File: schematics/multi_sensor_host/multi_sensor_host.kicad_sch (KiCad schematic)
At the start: 54 parts, among them J1 esp_rst, J10 swd, J11 stm_boot, J12 DC37_Receptacle_MountingHoles, J2 esp_flash_wifi, J3 esp_boot, J4 esp_flash_port, J5 tx, J6 MY_USB_B, J7 rst, J8 rx, J9 uart1, U8 MCP73812T-420I-OT, Y1 Crystal

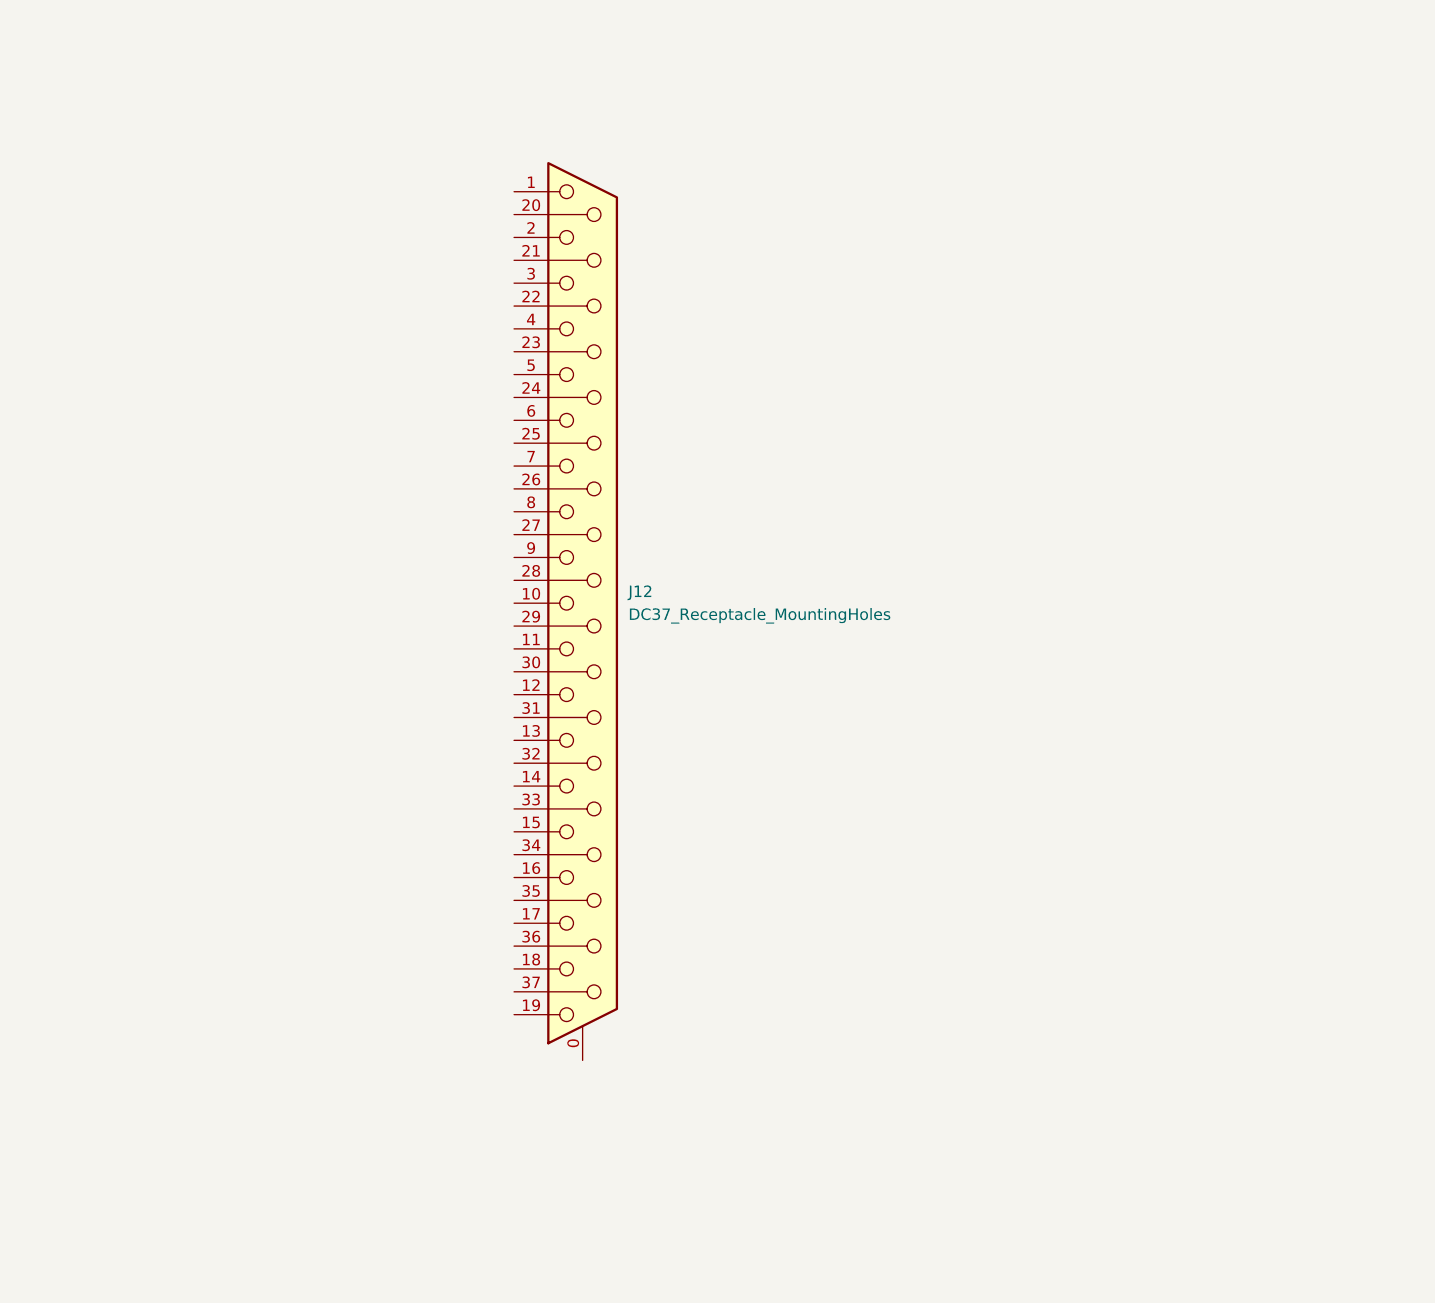
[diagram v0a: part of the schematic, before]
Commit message: Added two 27 pin sockets.
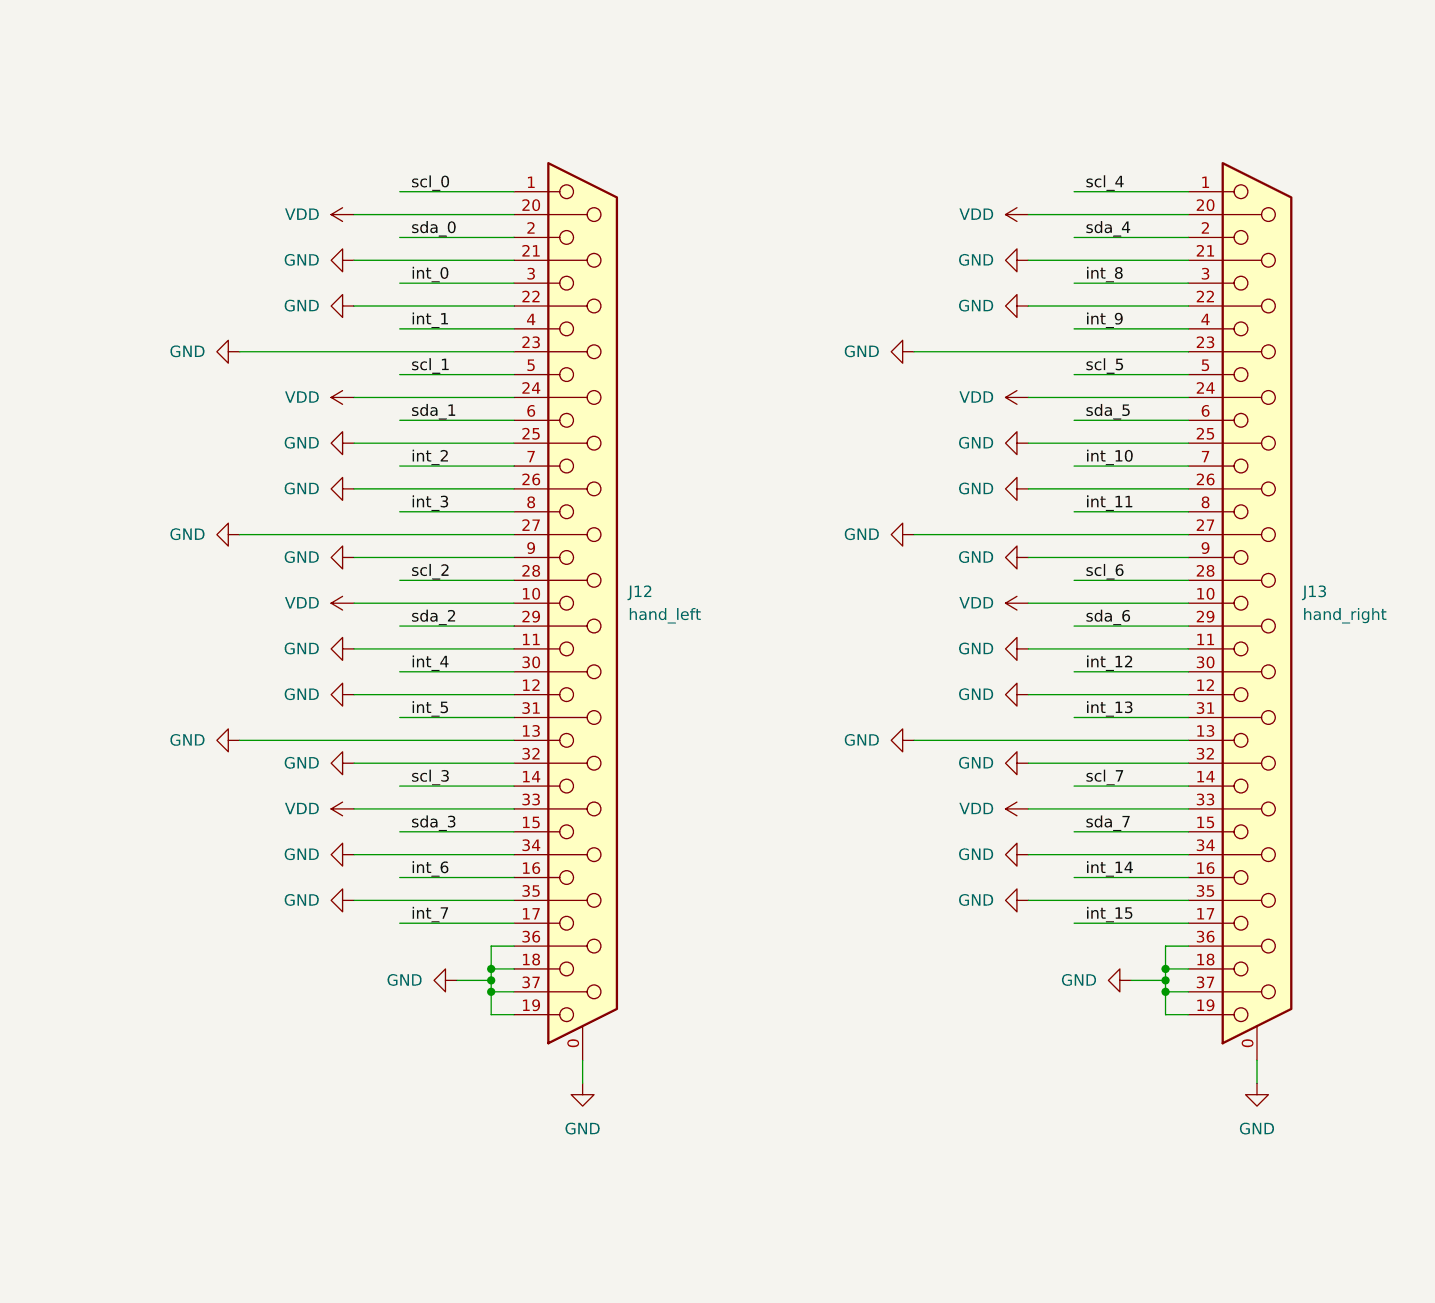
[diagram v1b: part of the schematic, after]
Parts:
- added J13: hand_right, symbol Connector:DC37_Receptacle_MountingHoles
- J12: value DC37_Receptacle_MountingHoles -> hand_left
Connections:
- net GND: now also J12.0 (PAD), J12.11, J12.12, J12.13, J12.18, J12.19, J12.21, J12.22, J12.23, J12.25, J12.26, J12.27, J12.32, J12.34, J12.35, J12.36, J12.37, J12.9, J13.0 (PAD), J13.11, J13.12, J13.13, J13.18, J13.19, J13.21, J13.22, J13.23, J13.25, J13.26, J13.27, J13.32, J13.34, J13.35, J13.36, J13.37, J13.9
- net VDD: now also J12.10, J12.20, J12.24, J12.33, J13.10, J13.20, J13.24, J13.33
- net int_0: now also J12.3
- net int_1: now also J12.4
- net int_10: now also J13.7
- net int_11: now also J13.8
- net int_12: now also J13.30
- net int_13: now also J13.31
- net int_14: now also J13.16
- net int_15: now also J13.17
- net int_2: now also J12.7
- net int_3: now also J12.8
- net int_5: now also J12.31
- net int_6: now also J12.16
- net int_7: now also J12.17
- net int_8: now also J13.3
- net int_9: now also J13.4
- net scl_0: now also J12.1
- net scl_1: now also J12.5
- net scl_2: now also J12.28
- net scl_3: now also J12.14
- net scl_4: now also J13.1
- net scl_5: now also J13.5
- net scl_6: now also J13.28
- net scl_7: now also J13.14
- net sda_0: now also J12.2
- net sda_1: now also J12.6
- net sda_2: now also J12.29
- net sda_3: now also J12.15
- net sda_4: now also J13.2
- net sda_5: now also J13.6
- net sda_6: now also J13.29
- net sda_7: now also J13.15
- net int_4: now reaches J12.30

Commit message: Added all 5 sockets.
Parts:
- added J14: leg_left, symbol Connector:DC37_Receptacle_MountingHoles
- added J15: leg_right, symbol Connector:DC37_Receptacle_MountingHoles
- added J16: torso_head, symbol Connector:DC37_Receptacle_MountingHoles
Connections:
- net GND: now also J14.0 (PAD), J14.18, J14.19, J14.21, J14.22, J14.23, J14.25, J14.26, J14.27, J14.36, J14.37, J15.0 (PAD), J15.18, J15.19, J15.21, J15.22, J15.23, J15.25, J15.26, J15.27, J15.36, J15.37, J16.0 (PAD), J16.11, J16.12, J16.13, J16.17, J16.18, J16.19, J16.21, J16.22, J16.23, J16.25, J16.26, J16.27, J16.32, J16.34, J16.35, J16.36, J16.37, J16.9; no longer J13.36
- net VDD: now also J14.20, J14.24, J15.20, J15.24, J16.10, J16.20, J16.24, J16.33
- net int_10: now also J13.8; no longer J13.7
- net int_11: now also J13.30; no longer J13.8
- net int_12: now also J13.31; no longer J13.30
- net int_13: now also J13.16; no longer J13.31
- net int_14: now also J14.3; no longer J13.16
- net int_15: now also J14.4; no longer J13.17
- net int_16: now also J14.7
- net int_17: now also J14.8
- net int_18: now also J15.3
- net int_19: now also J15.4
- net int_20: now also J15.7
- net int_21: now also J15.8
- net int_22: now also J16.3
- net int_23: now also J16.4
- net int_24: now also J16.7
- net int_25: now also J16.8
- net int_26: now also J16.30
- net int_27: now also J16.31
- net int_28: now also J16.16
- net int_29: now also J12.17
- net int_30: now also J13.17
- net int_31: now also J13.36
- net int_7: now also J13.3; no longer J12.17
- net int_8: now also J13.4; no longer J13.3
- net int_9: now also J13.7; no longer J13.4
- net scl_10: now also J15.1
- net scl_11: now also J15.5
- net scl_12: now also J16.1
- net scl_13: now also J16.5
- net scl_14: now also J16.28
- net scl_15: now also J16.14
- net scl_8: now also J14.1
- net scl_9: now also J14.5
- net sda_10: now also J15.2
- net sda_11: now also J15.6
- net sda_12: now also J16.2
- net sda_13: now also J16.6
- net sda_14: now also J16.29
- net sda_15: now also J16.15
- net sda_8: now also J14.2
- net sda_9: now also J14.6
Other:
- moved on the sheet: J12, J13

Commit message: No errors, no warnings.
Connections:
- net eps_tx is gone; now on net esp_tx: J4.3 (Pin_3), U7.16 (IO_1/UART0_TX)
- net GND: now also J14.10, J14.11, J14.12, J14.13, J14.14, J14.15, J14.16, J14.17, J14.28, J14.29, J14.30, J14.31, J14.32, J14.33, J14.34, J14.35, J14.9, J15.10, J15.11, J15.12, J15.13, J15.14, J15.15, J15.16, J15.17, J15.28, J15.29, J15.30, J15.31, J15.32, J15.33, J15.34, J15.35, J15.9

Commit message: Replaced ESP-21S with BM71 Microchip UART BLE module.
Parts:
- removed J1: esp_rst, symbol Connector:Conn_01x02_Pin
- removed J12: hand_left, symbol Connector:DC37_Receptacle_MountingHoles
- removed J13: hand_right, symbol Connector:DC37_Receptacle_MountingHoles
- removed J14: leg_left, symbol Connector:DC37_Receptacle_MountingHoles
- removed J15: leg_right, symbol Connector:DC37_Receptacle_MountingHoles
- removed J16: torso_head, symbol Connector:DC37_Receptacle_MountingHoles
- removed J2: esp_flash_wifi, symbol Connector:Conn_01x02_Pin
- removed J4: esp_flash_port, symbol Connector:Conn_01x04_Pin
- removed U7: ~, esp-12s:ESP-12S, symbol esp_12s:ESP-12S
- added C22, C32, C33, C34, C35: 4u7, Capacitors_SMD:C_0603, symbol Device:C
- added D5: LED, LED_THT:LED_D3.0mm, symbol Device:LED
- added J1, J18, J19, J2, J20, J21, J22, J23, J24, J25, J26, J27, J28, J29, J30, J4: RJ45, symbol Connector:RJ45
- added J17: bm_rst, symbol Connector:Conn_01x02_Pin
- added R96, R97: 10k, Resistors_SMD:R_0603, symbol Device:R
- added R98: 1k 5%, Resistor_SMD:R_0603_1608Metric, symbol Device:R
- added TP3: bm_cfg, symbol Connector:TestPoint
- added TP4: bm_vdd, symbol Connector:TestPoint
- added TP5: bm_tx, symbol Connector:TestPoint
- added TP6: bm_rx, symbol Connector:TestPoint
- added TP7: bm_gnd, symbol Connector:TestPoint
- added TP8: bm_rst, symbol Connector:TestPoint
- added U7: BM71BLES1FC2-0B02AA, BM71BLES1FC2_MCH, symbol BM71BLES1FC2:BM71BLES1FC2-0B02AA
- J3: value esp_boot -> bm_cfg
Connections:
- net GND: now also C22.2, C32.2, C33.2, C34.2, C35.2, J1.2, J1.4, J17.2 (Pin_2), J18.2, J18.4, J19.2, J19.4, J2.2, J2.4, J20.2, J20.4, J21.2, J21.4, J22.2, J22.4, J23.2, J23.4, J24.2, J24.4, J25.2, J25.4, J26.2, J26.4, J27.2, J27.4, J28.2, J28.4, J29.2, J29.4, J30.2, J30.4, J4.2, J4.4, TP7.1, U7.13 (GND), U7.2 (GND)
- net VDD: now also C33.1, C34.1, C35.1, J1.6, J1.8, J18.6, J18.8, J19.6, J19.8, J2.6, J2.8, J20.6, J20.8, J21.6, J21.8, J22.6, J22.8, J23.6, J23.8, J24.6, J24.8, J25.6, J25.8, J26.6, J26.8, J27.6, J27.8, J28.6, J28.8, J29.6, J29.8, J30.6, J30.8, J4.6, J4.8, R96.1, R97.1, R98.1, TP4.1, U7.14 (VBAT)
- net int_0: now also J1.5
- net int_1: now also J1.7
- net int_10: now also J20.7
- net int_11: now also J21.5
- net int_12: now also J21.7
- net int_13: now also J22.5
- net int_14: now also J23.5
- net int_15: now also J23.7
- net int_16: now also J24.5
- net int_17: now also J24.7
- net int_18: now also J25.5
- net int_19: now also J25.7
- net int_2: now also J2.5
- net int_20: now also J26.5
- net int_21: now also J26.7
- net int_22: now also J27.5
- net int_23: now also J27.7
- net int_24: now also J28.5
- net int_25: now also J28.7
- net int_26: now also J29.5
- net int_27: now also J29.7
- net int_28: now also J30.5
- net int_29: now also J30.7
- net int_3: now also J2.7
- net int_30: now also J18.7
- net int_31: now also J22.7
- net int_4: now also J4.5
- net int_5: now also J4.7
- net int_6: now also J18.5
- net int_7: now also J19.5
- net int_8: now also J19.7
- net int_9: now also J20.5
- net scl_0: now also J1.1
- net scl_1: now also J2.1
- net scl_10: now also J25.1
- net scl_11: now also J26.1
- net scl_12: now also J27.1
- net scl_13: now also J28.1
- net scl_14: now also J29.1
- net scl_15: now also J30.1
- net scl_2: now also J4.1
- net scl_3: now also J18.1
- net scl_4: now also J19.1
- net scl_5: now also J20.1
- net scl_6: now also J21.1
- net scl_7: now also J22.1
- net scl_8: now also J23.1
- net scl_9: now also J24.1
- net sda_0: now also J1.3
- net sda_1: now also J2.3
- net sda_10: now also J25.3
- net sda_11: now also J26.3
- net sda_12: now also J27.3
- net sda_13: now also J28.3
- net sda_14: now also J29.3
- net sda_15: now also J30.3
- net sda_2: now also J4.3
- net sda_3: now also J18.3
- net sda_4: now also J19.3
- net sda_5: now also J20.3
- net sda_6: now also J21.3
- net sda_7: now also J22.3
- net sda_8: now also J23.3
- net sda_9: now also J24.3
- net bm_cfg: now reaches J3.1 (Pin_1)
- net bm_cfg: now also R86.2, C22.1, TP3.1, U7.16 (P2_0)
- net esp_rx renamed bm_rx
- net bm_rx: now also R96.2, TP6.1, U7.7 (HCI_RXD); no longer R86.2
- net esp_tx renamed bm_tx
- net bm_tx: now also TP5.1, U7.8 (HCI_TXD)
- new net: D5.2 (A), R98.2
- new net bm_led: D5.1 (K), U7.12 (P0_2)
- new net bm_rst: C32.1, J17.1 (Pin_1), R97.2, TP8.1, U7.10 (RST_N)
- no-connect marks 39 -> 37
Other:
- note added: "Left arm"
- note added: "Left leg"
- note added: "Right arm"
- note added: "Right leg"
- note added: "Torso, neck, head."
- moved on the sheet: J3, J5, J8, R86

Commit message: Added power monitor. Split grounding and signals across ethernet cable twisted pairs.
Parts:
- removed U7: BM71BLES1FC2-0B02AA, BM71BLES1FC2_MCH, symbol BM71BLES1FC2:BM71BLES1FC2-0B02AA
- added J12: rst_cmn, symbol Connector:Conn_01x02_Pin
- added U11: ~, Package_TO_SOT_SMD:TSOT-23_HandSoldering, symbol mcp111:MCP111
- added U12: BM71BLES1FC2-0B02AA, BM71BLES1FC2_MCH, symbol BM71BLES1FC2:BM71BLES1FC2-0B02AA
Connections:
- net GND: now also J1.6, J18.6, J19.6, J2.6, J20.6, J21.6, J22.6, J23.6, J24.6, J25.6, J26.6, J27.6, J28.6, J29.6, J30.6, J4.6, U11.2 (Gnd), U12.13 (GND), U12.2 (GND); no longer J1.4, J18.4, J19.4, J2.4, J20.4, J21.4, J22.4, J23.4, J24.4, J25.4, J26.4, J27.4, J28.4, J29.4, J30.4, J4.4
- net VDD: now also J1.5, J18.5, J19.5, J2.5, J20.5, J21.5, J22.5, J23.5, J24.5, J25.5, J26.5, J27.5, J28.5, J29.5, J30.5, J4.5, U11.3 (Vdd), U12.14 (VBAT); no longer J1.6, J18.6, J19.6, J2.6, J20.6, J21.6, J22.6, J23.6, J24.6, J25.6, J26.6, J27.6, J28.6, J29.6, J30.6, J4.6
- net bm_cfg: now also U12.16 (P2_0)
- net bm_led: now also U12.12 (P0_2)
- net bm_rst: now also J12.1 (Pin_1), U11.1 (Vout), U12.10 (RST_N)
- net bm_rx: now also U12.7 (HCI_RXD)
- net bm_tx: now also U12.8 (HCI_TXD)
- net int_0: now also J1.4; no longer J1.5
- net int_11: now also J21.4; no longer J21.5
- net int_13: now also J22.4; no longer J22.5
- net int_14: now also J23.4; no longer J23.5
- net int_16: now also J24.4; no longer J24.5
- net int_18: now also J25.4; no longer J25.5
- net int_2: now also J2.4; no longer J2.5
- net int_20: now also J26.4; no longer J26.5
- net int_22: now also J27.4; no longer J27.5
- net int_24: now also J28.4; no longer J28.5
- net int_26: now also J29.4; no longer J29.5
- net int_28: now also J30.4; no longer J30.5
- net int_4: now also J4.4; no longer J4.5
- net int_6: now also J18.4; no longer J18.5
- net int_7: now also J19.4; no longer J19.5
- net int_9: now also J20.4; no longer J20.5
- net ~{mcu-rst}: now also J12.2 (Pin_2)
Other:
- note added: "Ethernet pairs are 1, 2 - orange 3, 6 - green 4, 5 - blue 7, 8 - brown"
- note added: "I probably need 3.08V version of this monitor. It is because for LiIon battery 3V is full discharge. And it is not good for it."
- moved on the sheet: C32, J17, R97
